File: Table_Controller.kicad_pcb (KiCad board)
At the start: 2 copper layers, 98 parts, among them J10 1050171001 Micro Type B, J11 HX JN1.27-2x5 WZ H4.9, J12 Conn_01x04_Pin, J13 Conn_01x14_Pin, J14 2.54 mm header, J15 2.54 mm header, U10 STM32G431K8Tx, U11 LMR380x0, U12 VNH7070, Y10 20 MHz

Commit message: sch drafted, missing power input connector
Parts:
- J11: footprint Personal:JN1.27-2x5 WZ H4.9 -> Personal:HX JN1.27-2x5P ZZ H4.9; moved to B.Cu
- moved C14 83.0 mm to (135.8, 86.8), turned to 180 degrees
- moved C16 77.6 mm to (135.8, 84.2), turned to 180 degrees
- moved D10 77.4 mm to (101.8, 115.4), turned to 180 degrees
- moved JP19 76.7 mm to (78.1, 77.3), turned to 180 degrees
- moved JP28 75.5 mm to (77.3, 81.6), turned to 180 degrees
- moved TP17 74.9 mm to (117.4, 86.6), turned to 180 degrees
- moved TP15 73.8 mm to (122.0, 77.3), turned to 180 degrees
- moved TP16 73.0 mm to (128.9, 75.8), turned to 180 degrees
- moved TP14 72.8 mm to (135.9, 77.3), turned to 180 degrees
- moved C18 70.8 mm to (135.6, 80.6), turned to -90 degrees
- moved TP13 69.0 mm to (125.5, 77.4), turned to 180 degrees
- moved TP28 66.0 mm to (103.6, 94.5)
- moved TP24 64.8 mm to (113.6, 84.4), turned to 180 degrees
- moved TP27 64.6 mm to (103.5, 98.0)
- moved C27 62.2 mm to (74.7, 73.5), turned to 90 degrees
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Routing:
- net /S3V3: track 310.9 -> 378.2 mm
- net /SWO: track 0.00 -> 31.3 mm
- net /SWDIO: track 0.00 -> 21.6 mm
- net /SWDCLK: track 0.00 -> 21.5 mm
- net /INa: track 0.00 -> 18.9 mm
- net /PWM: track 0.00 -> 17.3 mm
- net Net-(U10-PF1): track 0.00 -> 16.8 mm
- net /SEL0: track 0.00 -> 15.8 mm
- net /INb: track 0.00 -> 15.8 mm
- net /ENCa_filt: track 0.00 -> 14.2 mm
- net /ENCb_filt: track 0.00 -> 13.0 mm
- net /GND: track 0.00 -> 10.7 mm, vias 10 -> 24
- net /NRST: track 0.00 -> 10.6 mm
- net /MOT_CS: track 0.00 -> 10.3 mm
- net Net-(U10-PF0): track 0.00 -> 5.39 mm
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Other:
- board outline added: 141.6 x 116.3 mm

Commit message: placement started
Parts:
- moved TP19 48.8 mm to (103.2, 83.5), turned to -90 degrees
- moved TP20 44.9 mm to (99.5, 83.5), turned to -90 degrees
- moved C23 43.4 mm to (101.8, 123.0)
- moved TP18 41.9 mm to (98.0, 120.0)
- moved U12 39.1 mm to (101.5, 88.5), turned to -90 degrees
- moved TP22 38.5 mm to (103.5, 93.5), turned to -90 degrees
- moved R15 36.9 mm to (97.0, 123.0), turned to 180 degrees
- moved JP28 36.9 mm to (113.8, 87.5)
- moved JP22 36.7 mm to (82.0, 100.0)
- moved C32 36.7 mm to (88.4, 102.2)
- moved J14 36.7 mm to (85.3, 106.0)
- moved JP19 36.2 mm to (113.8, 83.5)
- moved C25 34.1 mm to (95.8, 52.8)
- moved C27 33.8 mm to (104.0, 56.8)
- moved TP23 33.7 mm to (93.0, 117.2)
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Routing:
- net /S19V5: track 0.00 -> 70.1 mm
- net /OUTa: track 0.00 -> 26.0 mm
- net Net-(C22-Pad1): track 0.00 -> 24.8 mm
- net /OUTb: track 0.00 -> 24.5 mm
- net /S3V3: track 378.2 -> 357.5 mm
- net /ENCa_filt: track 14.2 -> 27.7 mm
- net /ENCb_filt: track 13.0 -> 26.2 mm
- net Net-(U11-FB): track 0.00 -> 13.0 mm
- net Net-(U11-SW): track 0.00 -> 11.5 mm
- net /GND: track 10.7 -> 22.1 mm, vias 24 -> 29
- net Net-(U12-INa): track 0.00 -> 10.7 mm
- net /INb: track 15.8 -> 25.3 mm
- net /SEL0: track 15.8 -> 7.78 mm
- net /PWM: track 17.3 -> 11.0 mm
- net Net-(U12-INb): track 0.00 -> 5.68 mm
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
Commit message: Placement proposal 90%
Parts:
- removed JP10, JP11, JP12, JP13, JP14, JP20, JP21, JP22, JP23: 0R, Resistor_SMD:R_0603_1608Metric_Pad0.98x0.95mm_HandSolder
- removed JP18, JP28: 0R, Resistor_THT:R_Axial_DIN0204_L3.6mm_D1.6mm_P5.08mm_Horizontal
- added JP31: 0R, Resistor_THT:R_Axial_DIN0204_L3.6mm_D1.6mm_P5.08mm_Horizontal, F.Cu at (95.8, 77.5)
- added JP32: 0R, Resistor_THT:R_Axial_DIN0204_L3.6mm_D1.6mm_P7.62mm_Horizontal, B.Cu at (99.8, 96.2)
- added JP34: 0R, Personal:Jumper_0603, F.Cu at (118.5, 128.2)
- added JP35: 0R, Personal:Jumper_0603, F.Cu at (83.5, 91.2)
- added JP36: 0R, Personal:Jumper_0603, F.Cu at (128.2, 109.2)
- added JP37: 0R, Personal:Jumper_0603, F.Cu at (128.2, 113.0)
- added JP38: 0R, Personal:Jumper_0603, F.Cu at (130.4, 93.5)
- added JP39: 0R, Personal:Jumper_0603, F.Cu at (94.2, 138.5)
- added JP40: 0R, Personal:Jumper_0603, F.Cu at (96.5, 138.5)
- added JP41: 0R, Personal:Jumper_0603, F.Cu at (98.2, 138.4)
- added JP42: 0R, Personal:Jumper_0603, F.Cu at (117.8, 139.0)
- added JP43: 0R, Personal:Jumper_0603, F.Cu at (121.0, 138.6)
- added JP44: 0R, Personal:Jumper_0603, F.Cu at (113.0, 137.9)
- added JP45: 0R, Personal:Jumper_0603, F.Cu at (108.6, 104.2)
- added JP46: 0R, Personal:Jumper_0603, F.Cu at (118.2, 98.2)
- JP25, JP27: footprint Resistor_SMD:R_0603_1608Metric_Pad0.98x0.95mm_HandSolder -> Resistor_THT:R_Axial_DIN0204_L3.6mm_D1.6mm_P7.62mm_Horizontal
- JP26: footprint Resistor_SMD:R_0603_1608Metric_Pad0.98x0.95mm_HandSolder -> Resistor_THT:R_Axial_DIN0204_L3.6mm_D1.6mm_P7.62mm_Horizontal; moved to B.Cu
- moved C27 45.3 mm to (101.0, 102.0), turned to -90 degrees
- moved TP19 35.7 mm to (118.5, 115.8)
- moved JP25 31.8 mm to (95.2, 119.3), turned to 90 degrees
- moved C25 30.3 mm to (104.5, 81.8)
- moved TP20 24.8 mm to (108.2, 106.8)
- moved JP19 20.8 mm to (115.0, 104.2), turned to 0 degrees
- moved TP28 16.7 mm to (105.0, 109.2)
- moved TP21 11.3 mm to (110.5, 96.2)
- moved JP27 10.0 mm to (97.8, 89.8), turned to 0 degrees
- moved TP22 9.50 mm to (103.8, 103.0)
- moved TP23 8.55 mm to (95.2, 109.0)
- moved C35 7.95 mm to (130.0, 128.0), turned to 90 degrees
- moved U12 7.75 mm to (101.5, 96.2)
- moved C24 7.57 mm to (117.2, 86.0), turned to 90 degrees
- moved C36 7.33 mm to (130.0, 123.2), turned to -90 degrees
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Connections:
- net Net-(U10-PF0) renamed /XIN
- net Net-(U10-PF1) renamed /XOUT
- C25 pad 1: /S19V5 -> Net-(C25-Pad1)
- C27 pad 1: /S19V5 -> Net-(C25-Pad1)
- J11 pad 3: /SWO -> Net-(J11-Pin_3)
- JP19 pad 1: /SEL0 -> /SWO
- JP19 pad 2: Net-(U12-SEL0) -> Net-(J11-Pin_3)
- JP25 pad 1: /DISP_CS -> Net-(JP25-Pad1)
- JP25 pad 2: Net-(J13-Pin_3) -> Net-(U12-CS)
- JP26 pad 1: /INa -> Net-(U12-INb)
- JP26 pad 2: Net-(U12-INa) -> /INb
- JP27 pad 1: /INb -> /OUTa
- JP27 pad 2: Net-(U12-INb) -> Net-(JP27-Pad2)
- R15 pad 2: Net-(U12-CS) -> Net-(JP25-Pad1)
- R16 pad 1: Net-(U12-CS) -> Net-(JP25-Pad1)
- TP19 pad 1: Net-(U12-INa) -> /INa
- TP20 pad 1: Net-(U12-INb) -> /INb
- TP21 pad 1: Net-(U12-PWM) -> /PWM
- U10 pad 25: /INa -> /PWM
- U10 pad 27: /PWM -> /SEL0
- U10 pad 6: /SEL0 -> /INa
- U12 pad 12: /S19V5 -> Net-(C25-Pad1)
- U12 pad 15: /OUTa -> Net-(JP27-Pad2)
- U12 pad 2: /OUTa -> Net-(JP27-Pad2)
- U12 pad 4: /S19V5 -> Net-(C25-Pad1)
- U12 pad 5: /S19V5 -> Net-(C25-Pad1)
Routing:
- net /NRST: track 10.6 -> 36.2 mm, vias 0 -> 2
- net Net-(C25-Pad1): track 0.00 -> 24.4 mm
- net /SWO: track 33.7 -> 11.7 mm
- net Net-(U12-INa): track 10.7 -> 25.8 mm
- net /PWM: track 11.0 -> 25.6 mm
- net Net-(U12-CS): track 0.00 -> 14.4 mm
- net Net-(J14-Pin_4): track 0.00 -> 14.0 mm
- net /INb: track 25.3 -> 37.3 mm
- net Net-(J10-Shield): track 0.00 -> 11.5 mm
- net Net-(J11-Pin_3): track 0.00 -> 11.0 mm
- net Net-(U12-INb): track 5.68 -> 15.8 mm
- net Net-(JP27-Pad2): track 0.00 -> 9.65 mm
- net /TOP_EOT: track 0.00 -> 9.19 mm
- net /USB_DP: track 11.9 -> 21.0 mm
- net Net-(U12-SEL0): track 0.00 -> 8.78 mm
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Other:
- board size 141.6 x 116.3 mm -> 62.8 x 79.2 mm
- copper layers 2 -> 4

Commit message: placement 95%
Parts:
- removed JP31: 0R, Resistor_THT:R_Axial_DIN0204_L3.6mm_D1.6mm_P5.08mm_Horizontal
- removed JP35: 0R, Personal:Jumper_0603
- moved TP21 15.6 mm to (115.5, 111.0)
- moved TP27 11.0 mm to (102.0, 107.8)
- moved TP23 10.5 mm to (104.0, 103.2)
- moved JP46 8.92 mm to (116.5, 107.0)
- moved TP29 8.87 mm to (122.5, 122.8)
- moved C24 8.86 mm to (116.0, 94.8), turned to -90 degrees
- moved C31 7.38 mm to (88.3, 124.7)
- moved C29 6.80 mm to (90.2, 124.6), turned to -90 degrees
- moved TP24 6.79 mm to (127.2, 94.0)
- moved JP38 6.75 mm to (123.7, 93.5)
- moved R12 6.75 mm to (127.5, 79.1)
- moved R14 6.75 mm to (122.7, 79.2)
- moved C14 6.75 mm to (130.0, 90.0)
- moved C16 6.75 mm to (130.0, 87.4)
- moved C18 6.75 mm to (129.8, 83.8)
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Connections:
- C25 pad 1: Net-(C25-Pad1) -> /S19V5
- C27 pad 1: Net-(C25-Pad1) -> /S19V5
- J14 pad 4: Net-(J14-Pin_4) -> /S3V3
- U12 pad 12: Net-(C25-Pad1) -> /S19V5
- U12 pad 4: Net-(C25-Pad1) -> /S19V5
- U12 pad 5: Net-(C25-Pad1) -> /S19V5
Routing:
- net /S3V3: track 349.3 -> 304.7 mm
- net Net-(C25-Pad1): track 24.4 -> 0.00 mm
- net Net-(J14-Pin_4): track 14.0 -> 0.00 mm
- net /S19V5: track 62.1 -> 75.7 mm
- net /INa: track 29.2 -> 20.7 mm
- net Net-(U12-INa): track 25.8 -> 33.3 mm
- net /ENCa_filt: track 36.0 -> 28.8 mm
- net /BOT_filt: track 21.8 -> 15.6 mm
- net /OUTb: track 28.4 -> 23.5 mm
- net Net-(U12-INb): track 15.8 -> 12.2 mm
- net Net-(C22-Pad1): track 24.8 -> 28.0 mm
- net /ENCb_filt: track 34.3 -> 31.8 mm, vias 0 -> 1
- net Net-(JP25-Pad1): track 6.31 -> 8.85 mm
- net /USB_DP: track 21.0 -> 18.6 mm
- net /PWM: track 25.6 -> 23.3 mm
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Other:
- board size 62.8 x 79.2 mm -> 52 x 80 mm

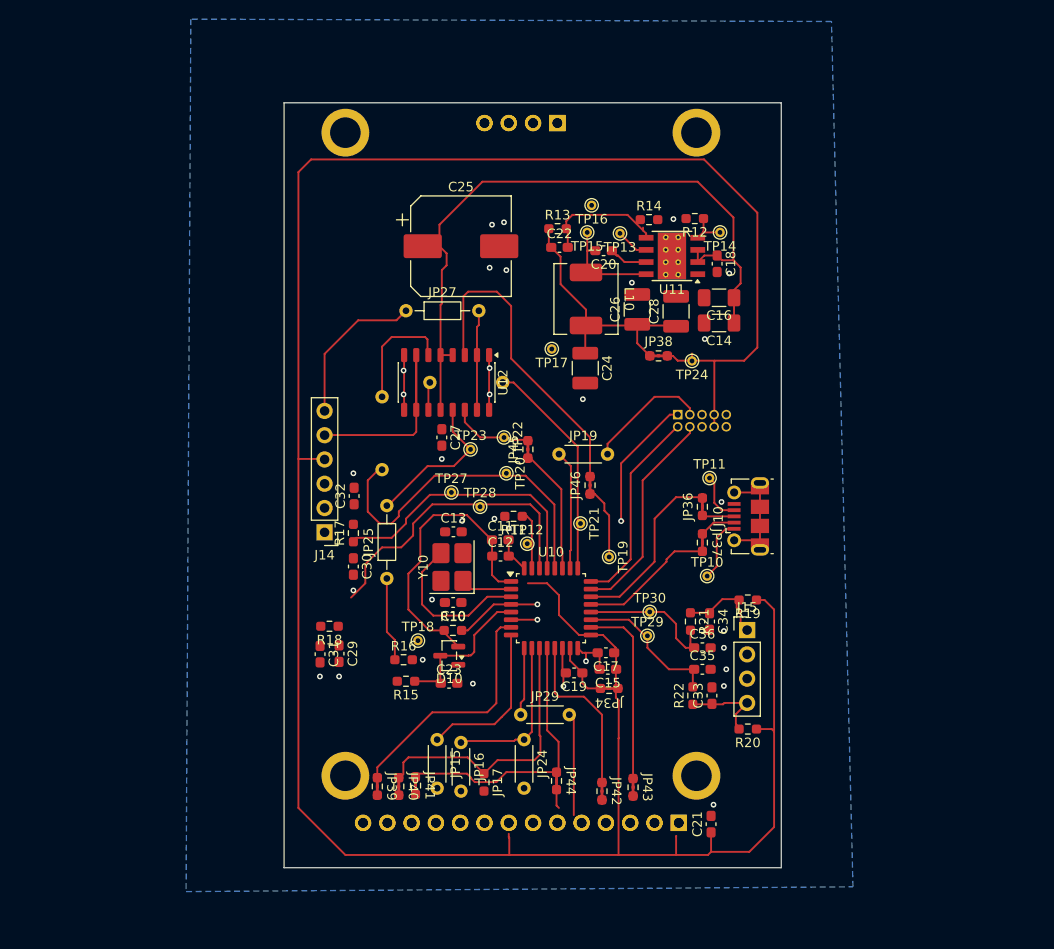
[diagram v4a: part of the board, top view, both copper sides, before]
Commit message: new usb connector
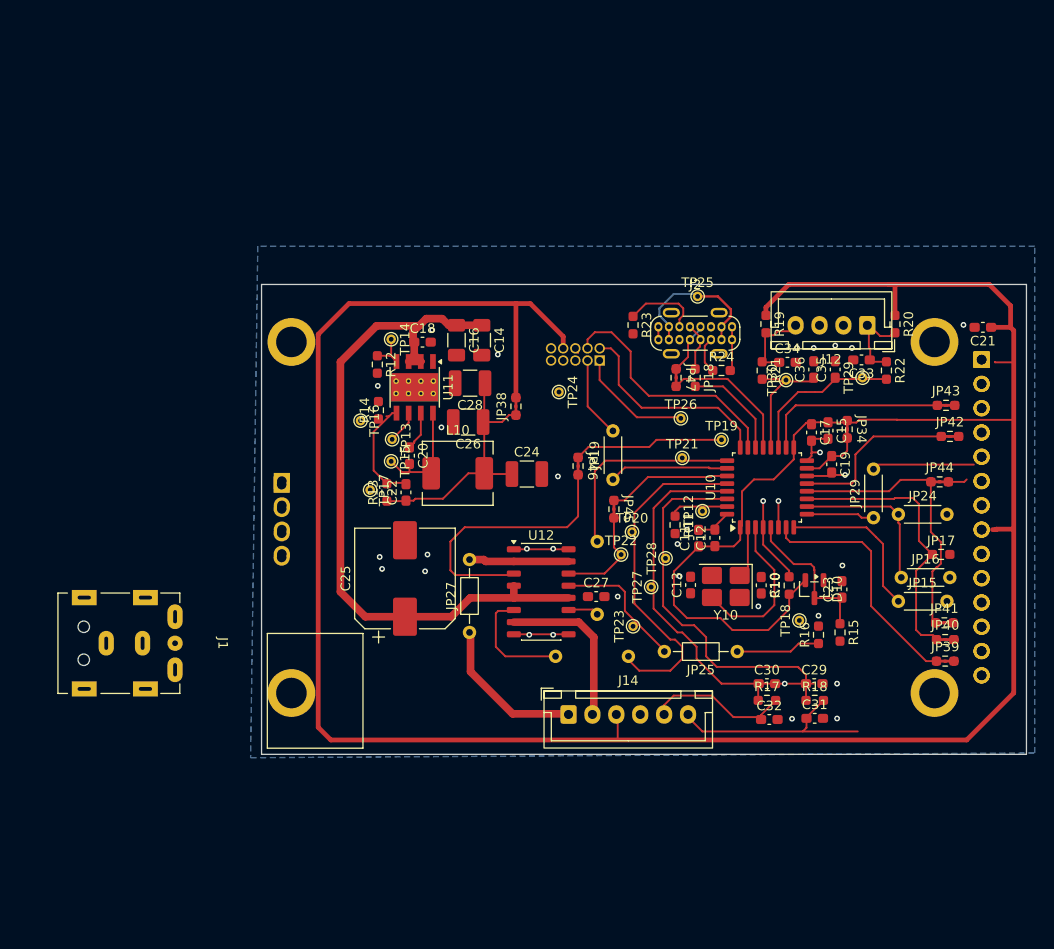
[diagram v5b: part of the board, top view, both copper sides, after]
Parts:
- removed J10: 1050171001 Micro Type B, Personal:USB_Micro-B_Molex-105017-0001
- removed JP36, JP37: 0R, Personal:Jumper_0603
- removed TP10, TP11: TestPoint, TestPoint:TestPoint_THTPad_D1.0mm_Drill0.5mm
- added J1: Dell DC jack, Personal:Dell DC jack, F.Cu at (60.9, 123.5)
- added J2: USB_C_Receptacle_USB2.0_16P, Personal:USB_C_socket_16P_vertical, F.Cu at (127.5, 91.1)
- added JP18: 0R, Resistor_SMD:R_0603_1608Metric_Pad0.98x0.95mm_HandSolder, F.Cu at (127.5, 95.8)
- added JP47: 0R, Personal:Jumper_0603, F.Cu at (125.5, 95.8)
- added R23: 5k1, Resistor_SMD:R_0603_1608Metric_Pad0.98x0.95mm_HandSolder, F.Cu at (121.0, 90.2)
- added R24: 5k1, Resistor_SMD:R_0603_1608Metric_Pad0.98x0.95mm_HandSolder, F.Cu at (130.2, 95.0)
- added TP25: TestPoint, TestPoint:TestPoint_THTPad_D1.0mm_Drill0.5mm, F.Cu at (127.8, 87.2)
- added TP26: TestPoint, TestPoint:TestPoint_THTPad_D1.0mm_Drill0.5mm, F.Cu at (126.0, 100.0)
- J11: footprint Personal:HX JN1.27-2x5P ZZ H4.9 -> Personal:JN1.27-2x5 WZ H4.9
- J12: value Conn_01x04_Pin -> JST B4B XH A; footprint Connector_PinSocket_2.54mm:PinSocket_1x04_P2.54mm_Vertical -> Connector_JST:JST_XH_B4B-XH-A_1x04_P2.50mm_Vertical; moved to F.Cu
- J14: value 2.54 mm header -> JST B6B XH A; footprint Connector_PinHeader_2.54mm:PinHeader_1x06_P2.54mm_Vertical -> Connector_JST:JST_XH_B6B-XH-A_1x06_P2.50mm_Vertical
- J15: moved to B.Cu
- moved JP39 60.8 mm to (153.6, 125.4), turned to 0 degrees
- moved C21 59.2 mm to (157.6, 90.5), turned to 180 degrees
- moved JP40 59.2 mm to (153.6, 123.1), turned to 0 degrees
- moved J13 57.9 mm to (157.5, 93.9), turned to 180 degrees
- moved JP41 57.9 mm to (153.6, 121.4), turned to 0 degrees
- moved JP17 53.4 mm to (153.2, 114.2), turned to 0 degrees
- moved C31 52.2 mm to (140.0, 131.4), turned to 0 degrees
- moved JP42 52.0 mm to (154.1, 101.9), turned to 0 degrees
- moved JP43 51.6 mm to (153.7, 98.6), turned to 0 degrees
- moved R18 51.3 mm to (140.0, 129.5), turned to 0 degrees
- moved J15 51.0 mm to (84.2, 106.9), turned to 180 degrees
- moved JP44 50.8 mm to (153.1, 106.6), turned to 0 degrees
- moved JP15 50.4 mm to (148.7, 119.1), turned to 0 degrees
- moved C29 49.8 mm to (139.9, 127.8), turned to 0 degrees
- moved C32 49.3 mm to (135.2, 131.5), turned to 0 degrees
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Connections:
- net Net-(JP27-Pad2) renamed /OUTa'
- net Net-(U12-CS) renamed /CS'
- net Net-(U12-INa) renamed /INa'
- net Net-(U12-INb) renamed /INb'
- net Net-(U12-PWM) renamed /PWM'
- net Net-(U12-SEL0) renamed /SEL0'
- J12 pad 1: unconnected-(J12-Pin_1-Pad1) -> /BOT_EOT
- J12 pad 2: unconnected-(J12-Pin_2-Pad2) -> /GND
- J12 pad 3: unconnected-(J12-Pin_3-Pad3) -> /GND
- J12 pad 4: unconnected-(J12-Pin_4-Pad4) -> /TOP_EOT
- J14 pad 1: /ENCb -> /OUTa
- J14 pad 2: /ENCa -> /OUTb
- J14 pad 3: /GND -> /S3V3
- J14 pad 4: /S3V3 -> /GND
- J14 pad 5: /OUTb -> /ENCa
- J14 pad 6: /OUTa -> /ENCb
- J15 pad 1: /TOP_EOT -> unconnected-(J15-Pin_1-Pad1)
- J15 pad 2: /GND -> unconnected-(J15-Pin_2-Pad2)
- J15 pad 3: /GND -> unconnected-(J15-Pin_3-Pad3)
- J15 pad 4: /BOT_EOT -> unconnected-(J15-Pin_4-Pad4)
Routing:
- net /ENCb: track 0.00 -> 23.2 mm
- net Net-(J2-VBUS-PadA4): track 0.00 -> 16.0 mm
- net /ENCa: track 0.00 -> 15.2 mm
- net /ENCa_filt: track 28.8 -> 41.4 mm
- net Net-(J10-Shield): track 11.5 -> 0.00 mm
- net Net-(J2-CC1): track 0.00 -> 8.10 mm
- net /USB_DP: track 18.6 -> 10.7 mm
- net /ENCb_filt: track 31.8 -> 39.3 mm, vias 1 -> 0
- net /INa: track 20.7 -> 27.7 mm
- net Net-(J10-VBUS): track 6.63 -> 0.00 mm
- net /OUTb: track 23.5 -> 17.0 mm
- net /GND: track 24.6 -> 30.6 mm
- net Net-(J2-D--PadA7): track 0.00 -> 5.47 mm
- net Net-(J10-ID): track 5.19 -> 0.00 mm
- net Net-(J2-D+-PadA6): track 0.00 -> 5.10 mm
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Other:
- board size 52 x 80 mm -> 80 x 49.1 mm
